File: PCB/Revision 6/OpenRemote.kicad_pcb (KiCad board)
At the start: 2 copper layers, 192.4 x 50 mm, 196 parts, among them J1 USB_C_Receptacle_USB2.0, J2 Conn_01x50, J3 JST_PH_B2B-PH, J4 2.54x2 Header, J5 Micro_SD_Card, J6 ER-CON06HB-1_TOUCH, J7 JST_PH_B2B-PH, Q1 DMG2301L, Q2 MBT3904DW1, Q3 DMG2301L, Q4 DMG2301L, Q5 DMG2301L, Q6 FS8205A, Q7 DMG2301L, U1 DW01A, U10 APX803S, U11 TP4056, U12 TCA8418, U2 XC6220B331, U3 CH340C, U4 USBLC6-2P6, U5 LIS3DHTR, U6 TSSP77038, U7 ESP32-S3-WROOM-1-N16R8, U8 AP2112K-3.3, U9 MAX17048G

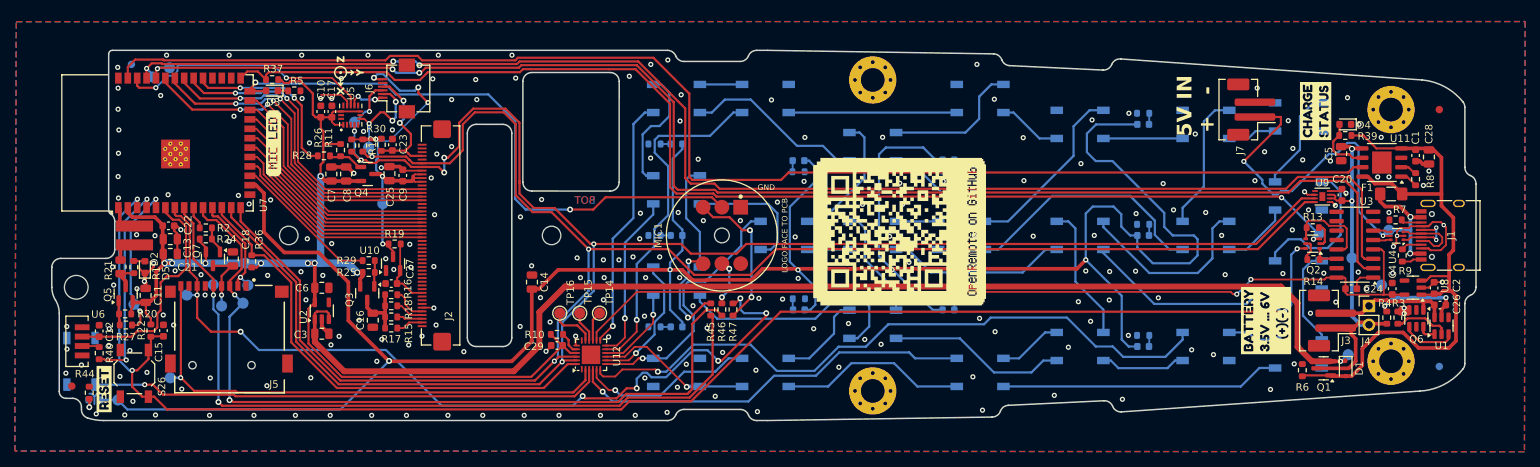
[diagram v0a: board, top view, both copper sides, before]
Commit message: Sync Rev 6 hardware work from workstation
PCB (Revision 6):
- J3 battery connector polarity update; the old KiBuzzard "(+)(-)"
  silkscreen graphic is replaced by a plain "Battery" F.Silkscreen label
- J3 nudged 0.1 mm in X
- Regenerated gerber.zip from the current board (kicad-cli 10.0.4)
- U5 (LIS3DHTR) now marked DNP; C14/C27/U10 added as DNP
- CPL.csv and BOM.xlsx left as-is pending regeneration

Also adds previously unpublished work from the workstation: Case Rev6
and Dock Rev6 CAD, Fusion scripts, PCB imports, Dock Rev6 board and
scripts, and Rev6 render images.

Co-Authored-By: Claude Opus 5 <noreply@anthropic.com>
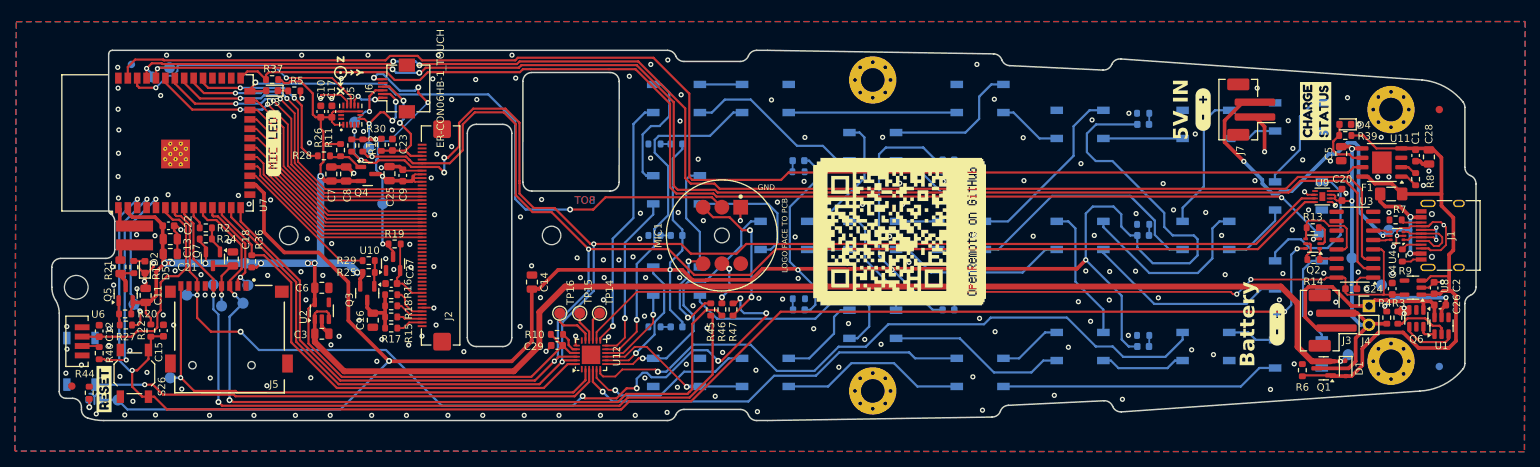
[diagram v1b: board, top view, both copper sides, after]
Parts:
- removed kibuzzard-643EE8B3: G***, kibuzzard-643EE8B3
- added kibuzzard-63D97EAF: G***, kibuzzard-63D97EAF, F.Cu at (207.5, 85.0)
- kibuzzard-63D97EAF: moved to F.Cu
- moved kibuzzard-63D97EAF 9.83 mm to (217.5, 114.0), turned to -90 degrees
- moved J3 0.10 mm to (225.0, 113.5)
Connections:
- D3 pad 2: MIC_VDD -> Net-(D3-A)
- J3 pad 1: +BATT -> -BATT
- J3 pad 2: -BATT -> +BATT
- J7 pad 1: /VUSB_RAW -> GND
- J7 pad 2: GND -> /VUSB_RAW
- U7 pad 26: MIC_VDD -> Net-(D3-A)
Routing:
- net -BATT: track 17.2 -> 30.7 mm
- net GND: track 84.1 -> 93.3 mm
- net +BATT: track 51.3 -> 52.3 mm
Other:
- board text added: "Battery"
- board text removed: "+ -"

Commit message: Merge MIC_VDD with IO45 net and regenerate Rev6 gerbers
Schematic:
- Added the missing 10.16 mm wire from (281.94, 69.85) to the MIC_VDD
  global label at (292.10, 69.85). The label had been drawn but never
  landed on the net, so MIC_VDD and Net-(D3-A) were two separate nets
  joined only by a track physically overlapping U7 pad 26 and D3 pad 2.
- MIC_VDD now carries D3.2, MIC1.2 and U7.26 (IO45); Net-(D3-A) is gone.

PCB:
- Netlist re-imported; MIC1 pin 6 grounded via a track to a new GND via
  at (145.50, 104.50) landing in the B.Cu plane; MIC_VDD routed properly.
- DRC errors 51 -> 44: all 4 shorting_items cleared, solder_mask_bridge
  9 -> 4 (remaining four are the fiducials).
- Regenerated gerber.zip from the current board (kicad-cli 10.0.4).
  Changes confined to F.Cu, B.Cu and one new PTH via; silkscreen, mask,
  paste and edge cuts are byte-identical to the previous set.

Also adds Dock Rev6 production files and the pogo-pin case STL.

Known outstanding: 11 clearance violations remain in the J7 5V-in and
J3 battery routing, tightest 0.100 mm, below JLCPCB's 0.127 mm minimum.
CPL.csv and BOM.xlsx are unchanged and still need regeneration.

Co-Authored-By: Claude Opus 5 <noreply@anthropic.com>
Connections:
- D3 pad 2: Net-(D3-A) -> MIC_VDD
- U7 pad 26: Net-(D3-A) -> MIC_VDD
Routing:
- net GND: track 93.3 -> 96.7 mm, vias 245 -> 246
